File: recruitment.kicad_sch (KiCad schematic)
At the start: 3 parts, among them K1 Relay_SPST_Latching_2coil

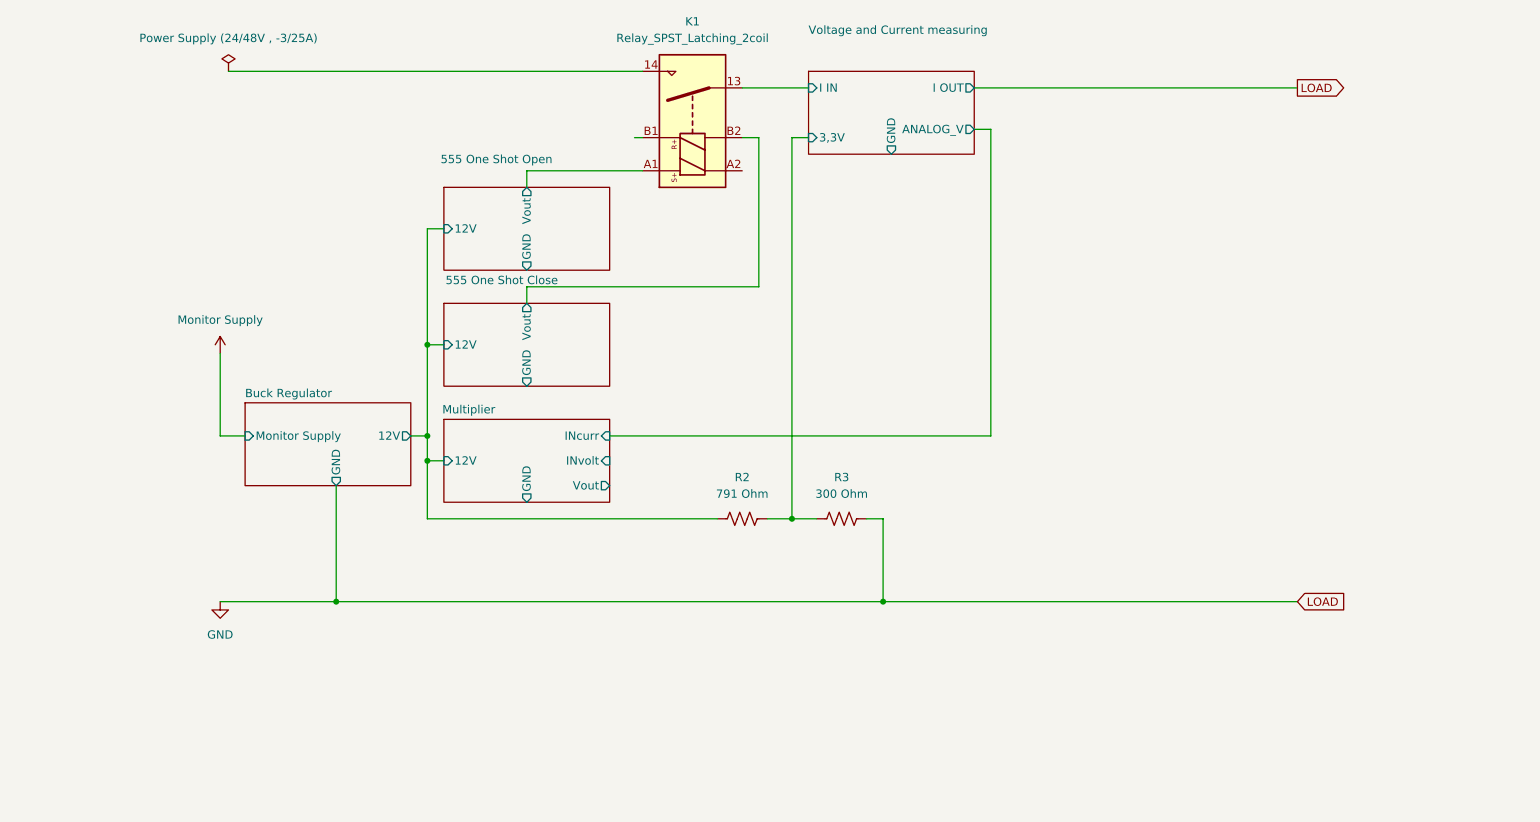
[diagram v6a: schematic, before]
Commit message: Added
Added voltage divider to sample Power Supply's voltage
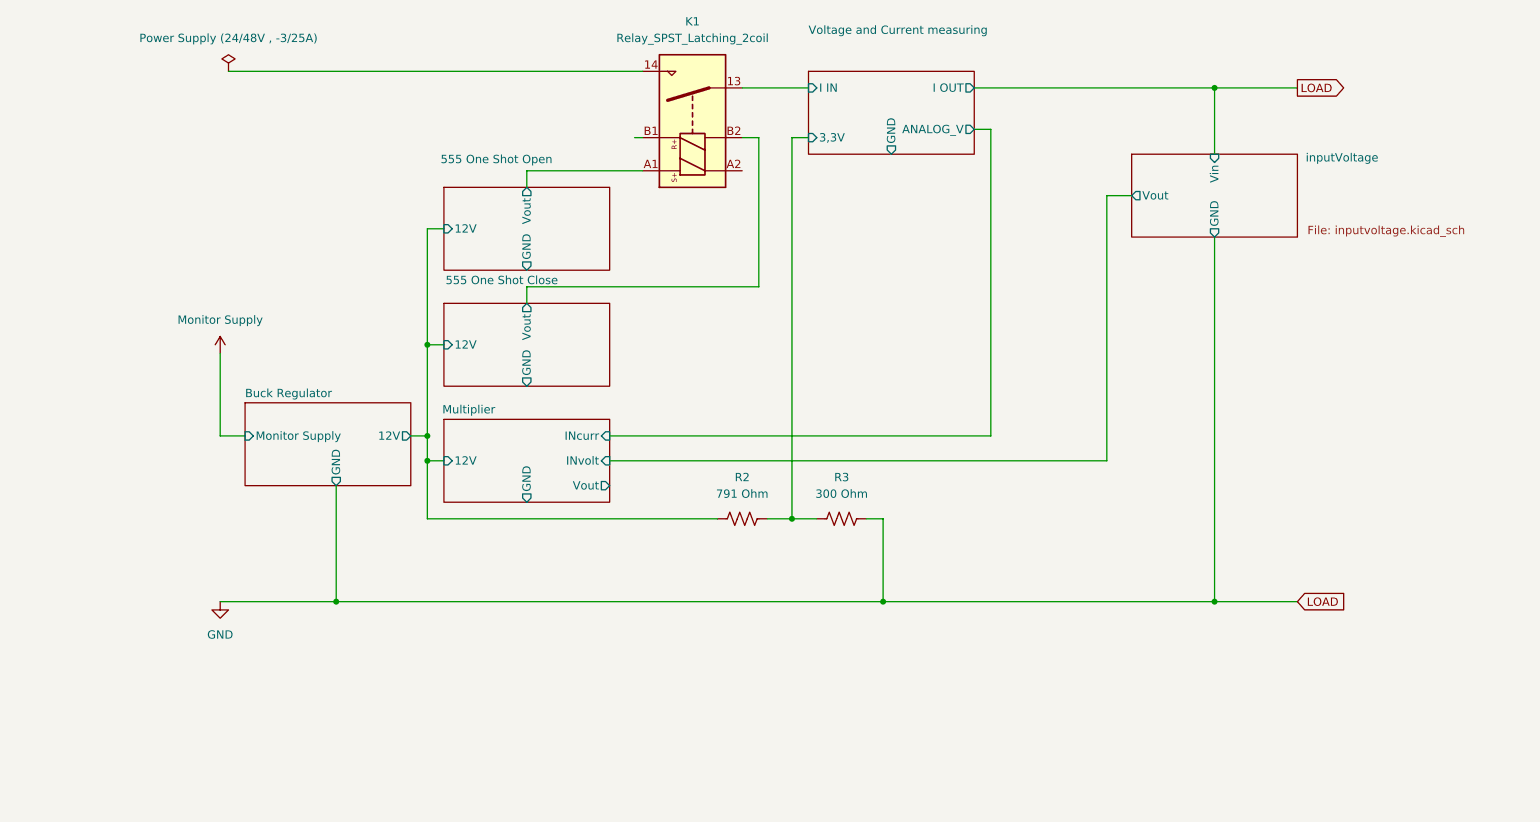
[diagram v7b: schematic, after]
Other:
- added sheet inputVoltage (inputvoltage.kicad_sch)
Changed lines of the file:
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@@
+	)
+	(junction
+		(at 215.9 40.64)
+		(diameter 0)
+		(color 0 0 0 0)
 	)
 	(junction
@@
 	)
 	(junction
+		(at 215.9 119.38)
+		(diameter 0)
+		(color 0 0 0 0)
+	)
+	(junction
 		(at 151.13 106.68)
 		(diameter 0)
@@
 	(wire
 		(pts
+			(xy 215.9 40.64) (xy 228.6 40.64)
+		)
+		(stroke
+			(width 0)
+			(type default)
+		)
+	)
+	(wire
+		(pts
 			(xy 63.5 119.38) (xy 81.28 119.38)
 		)
@@
 	(wire
 		(pts
-			(xy 165.1 119.38) (xy 228.6 119.38)
+			(xy 165.1 119.38) (xy 215.9 119.38)
 		)
 		(stroke
@@
 	(wire
 		(pts
+			(xy 215.9 119.38) (xy 228.6 119.38)
+		)
+		(stroke
+			(width 0)
+			(type default)
+		)
+	)
+	(wire
+		(pts
 			(xy 92.71 93.98) (xy 95.25 93.98)
 		)
@@
 	(wire
 		(pts
+			(xy 199.39 57.15) (xy 199.39 97.79)
+		)
+		(stroke
+			(width 0)
+			(type default)
+		)
+	)
+	(wire
+		(pts
 			(xy 165.1 106.68) (xy 165.1 119.38)
 		)
@@
 	(wire
 		(pts
+			(xy 215.9 63.5) (xy 215.9 119.38)
+		)
+		(stroke
+			(width 0)
+			(type default)
+		)
+	)
+	(wire
+		(pts
 			(xy 95.25 106.68) (xy 95.25 97.79)
 		)
@@
 	(wire
 		(pts
+			(xy 199.39 97.79) (xy 123.19 97.79)
+		)
+		(stroke
+			(width 0)
+			(type default)
+		)
+	)
+	(wire
+		(pts
+			(xy 215.9 40.64) (xy 215.9 50.8)
+		)
+		(stroke
+			(width 0)
+			(type default)
+		)
+	)
+	(wire
+		(pts
 			(xy 110.49 53.34) (xy 110.49 55.88)
 		)
@@
 	(wire
 		(pts
+			(xy 203.2 57.15) (xy 199.39 57.15)
+		)
+		(stroke
+			(width 0)
+			(type default)
+		)
+	)
+	(wire
+		(pts
 			(xy 97.79 62.23) (xy 95.25 62.23)
 		)
@@
 	(wire
 		(pts
-			(xy 179.07 40.64) (xy 228.6 40.64)
+			(xy 179.07 40.64) (xy 215.9 40.64)
 		)
 		(stroke
@@
 				)
 			)
+		)
+	)
+	(sheet
+		(at 203.2 50.8)
+		(size 25.4 12.7)
+		(exclude_from_sim no)
+		(in_bom yes)
+		(on_board yes)
+		(dnp no)
+		(stroke
+			(width 0.1524)
+			(type solid)
+		)
+		(fill
+			(color 0 0 0 0.0000)
+		)
+		(property "Sheetname" "inputVoltage"
+			(at 229.87 52.07 0)
+			(effects
+				(font
+					(size 1.27 1.27)
+				)
+				(justify left bottom)
+			)
+		)
+		(property "Sheetfile" "inputvoltage.kicad_sch"
+			(at 230.124 61.722 0)
+			(effects
+				(font
+					(size 1.27 1.27)
+				)
+				(justify left top)
+			)
+		)
+		(pin "GND" output
+			(at 215.9 63.5 270)
+			(effects
+				(font
+					(size 1.27 1.27)
+				)
+				(justify left)
+			)
+		)
+		(pin "Vin" input
+			(at 215.9 50.8 90)
+			(effects
+				(font
+					(size 1.27 1.27)
+				)
+				(justify right)
+			)
+		)
+		(pin "Vout" output
+			(at 203.2 57.15 180)
+			(effects
+				(font
+					(size 1.27 1.27)
+				)
+				(justify left)
+			)
+		)
+		(instances
+			(project "recruitment"
+				(path "/bdc7face-9f7c-4701-80bb-4cc144448db1"
+					(page "7")
+				)
+			)

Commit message: Temp Update
Added comments, Op Amp, changed tags, added some wiring, prepared for finalization of Schematic.
(Still missing some values)
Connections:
- net GND: now also K1.B1
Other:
- sheet Multiplier renamed Multiplier and Comparator
- added sheet INcurrent correction (incurrentCorrection.kicad_sch)
